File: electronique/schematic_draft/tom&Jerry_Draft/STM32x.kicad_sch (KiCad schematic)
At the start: 44 parts, among them J501 Conn_ST_STDC14, SW501 SW_Push, SW502 SW_Push, SW503 SW_Push, U501 STM32G431CBU6, Y501 16MHz

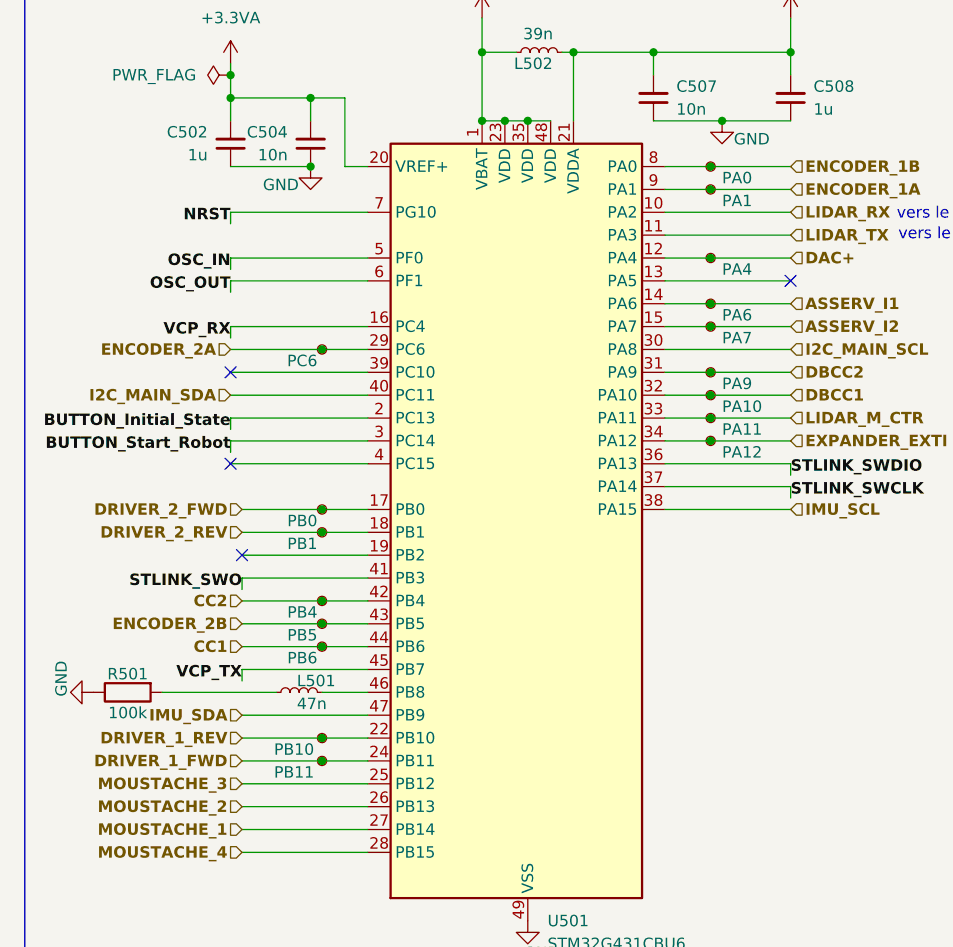
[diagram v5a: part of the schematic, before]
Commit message: V2.0 placement avec tout dessus
Aucun routage réalisé
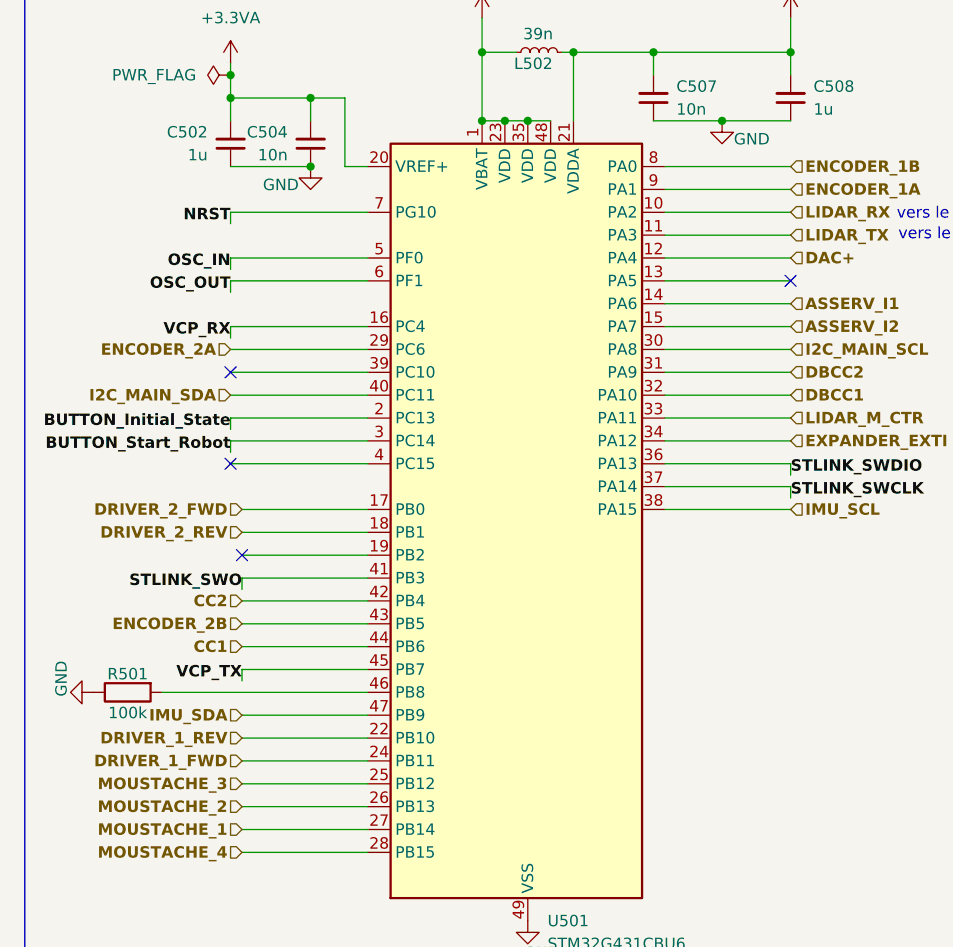
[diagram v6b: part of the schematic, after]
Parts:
- removed L501: 47n, Inductor_SMD:L_0603_1608Metric_Pad1.05x0.95mm_HandSolder, symbol Device:L_Small
- removed TP501: PC6, Test_Point:TestPoint_Pad_D1.5mm, symbol Connector:TestPoint_Small
- removed TP502: PB0, Test_Point:TestPoint_Pad_D1.5mm, symbol Connector:TestPoint_Small
- removed TP503: PB1, Test_Point:TestPoint_Pad_D1.5mm, symbol Connector:TestPoint_Small
- removed TP504: PB4, Test_Point:TestPoint_Pad_D1.5mm, symbol Connector:TestPoint_Small
- removed TP505: PB5, Test_Point:TestPoint_Pad_D1.5mm, symbol Connector:TestPoint_Small
- removed TP506: PB6, Test_Point:TestPoint_Pad_D1.5mm, symbol Connector:TestPoint_Small
- removed TP507: PB10, Test_Point:TestPoint_Pad_D1.5mm, symbol Connector:TestPoint_Small
- removed TP508: PB11, Test_Point:TestPoint_Pad_D1.5mm, symbol Connector:TestPoint_Small
- removed TP509: PA0, Test_Point:TestPoint_Pad_D1.5mm, symbol Connector:TestPoint_Small
- removed TP510: PA1, Test_Point:TestPoint_Pad_D1.5mm, symbol Connector:TestPoint_Small
- removed TP511: PA4, Test_Point:TestPoint_Pad_D1.5mm, symbol Connector:TestPoint_Small
- removed TP512: PA6, Test_Point:TestPoint_Pad_D1.5mm, symbol Connector:TestPoint_Small
- removed TP513: PA7, Test_Point:TestPoint_Pad_D1.5mm, symbol Connector:TestPoint_Small
- removed TP514: PA9, Test_Point:TestPoint_Pad_D1.5mm, symbol Connector:TestPoint_Small
- removed TP515: PA10, Test_Point:TestPoint_Pad_D1.5mm, symbol Connector:TestPoint_Small
- removed TP516: PA11, Test_Point:TestPoint_Pad_D1.5mm, symbol Connector:TestPoint_Small
- removed TP517: PA12, Test_Point:TestPoint_Pad_D1.5mm, symbol Connector:TestPoint_Small
- Y501: footprint Crystal:Crystal_SMD_3225-4Pin_3.2x2.5mm -> Crystal:Crystal_SMD_EuroQuartz_MT-4Pin_3.2x2.5mm
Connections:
- net at R501.2: now also U501.46 (PB8)

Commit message: Routage Signal Complet - PCB V2.0
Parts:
- renumbered C511 to C501, C507 to C502, C508 to C503, C510 to C504, C502 to C505, C504 to C506, C513 to C507, C512 to C508, C514 to C509, C501 to C510, C503 to C511, C505 to C512, C506 to C513, L502 to L501, R502 to R501, R501 to R502, R504 to R503, R506 to R504, R503 to R505, R505 to R506, SW502 to SW501, SW501 to SW502
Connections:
- net BUTTON_Initial_State: now also U501.3 (PC14); no longer U501.2 (PC13)
- net BUTTON_Start_Robot: now also U501.2 (PC13); no longer U501.3 (PC14)
- net DRIVER_2_FWD: now also U501.18 (PB1); no longer U501.17 (PB0)
- net DRIVER_2_REV: now also U501.17 (PB0); no longer U501.18 (PB1)
- net ENCODER_1A: now also U501.8 (PA0); no longer U501.9 (PA1)
- net ENCODER_1B: now also U501.9 (PA1); no longer U501.8 (PA0)
- net ENCODER_2A: now also U501.43 (PB5); no longer U501.29 (PC6)
- net ENCODER_2B: now also U501.29 (PC6); no longer U501.43 (PB5)
- net MOUSTACHE_1: now also U501.25 (PB12); no longer U501.27 (PB14)
- net MOUSTACHE_3: now also U501.27 (PB14); no longer U501.25 (PB12)
